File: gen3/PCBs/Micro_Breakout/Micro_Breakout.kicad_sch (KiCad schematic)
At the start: 50 parts, among them J1 BlueRobotics Depth Sensor, J10 Kill Switch, J11 StarOddi CTD Comms, J12 LED1, J13 LED2, J14 Leak Sensor, J15 Extra I2C #3, J16 Extra I2C #6, J17 Extra I2C #5, J18 Extra I2C #4, J19 GND Line, J2 Interconnect, J20 3.3V Line, J21 5V Line, J22 Extra SPI #1, J23 Extra SPI #2, J24 Extra SPI #3, J25 Secondary UART, J3 External Battery, J4 Conn_01x24, J5 External I2C, J6 Conn_01x24, J7 Extra I2C #1, J8 Extra I2C #2, J9 Lumen PWM, Q7 L78M05ABDT-TR, U15 AMS1117-3.3, U2 MCP9808_MSOP, U4 BME280, U6 Teensy4.1

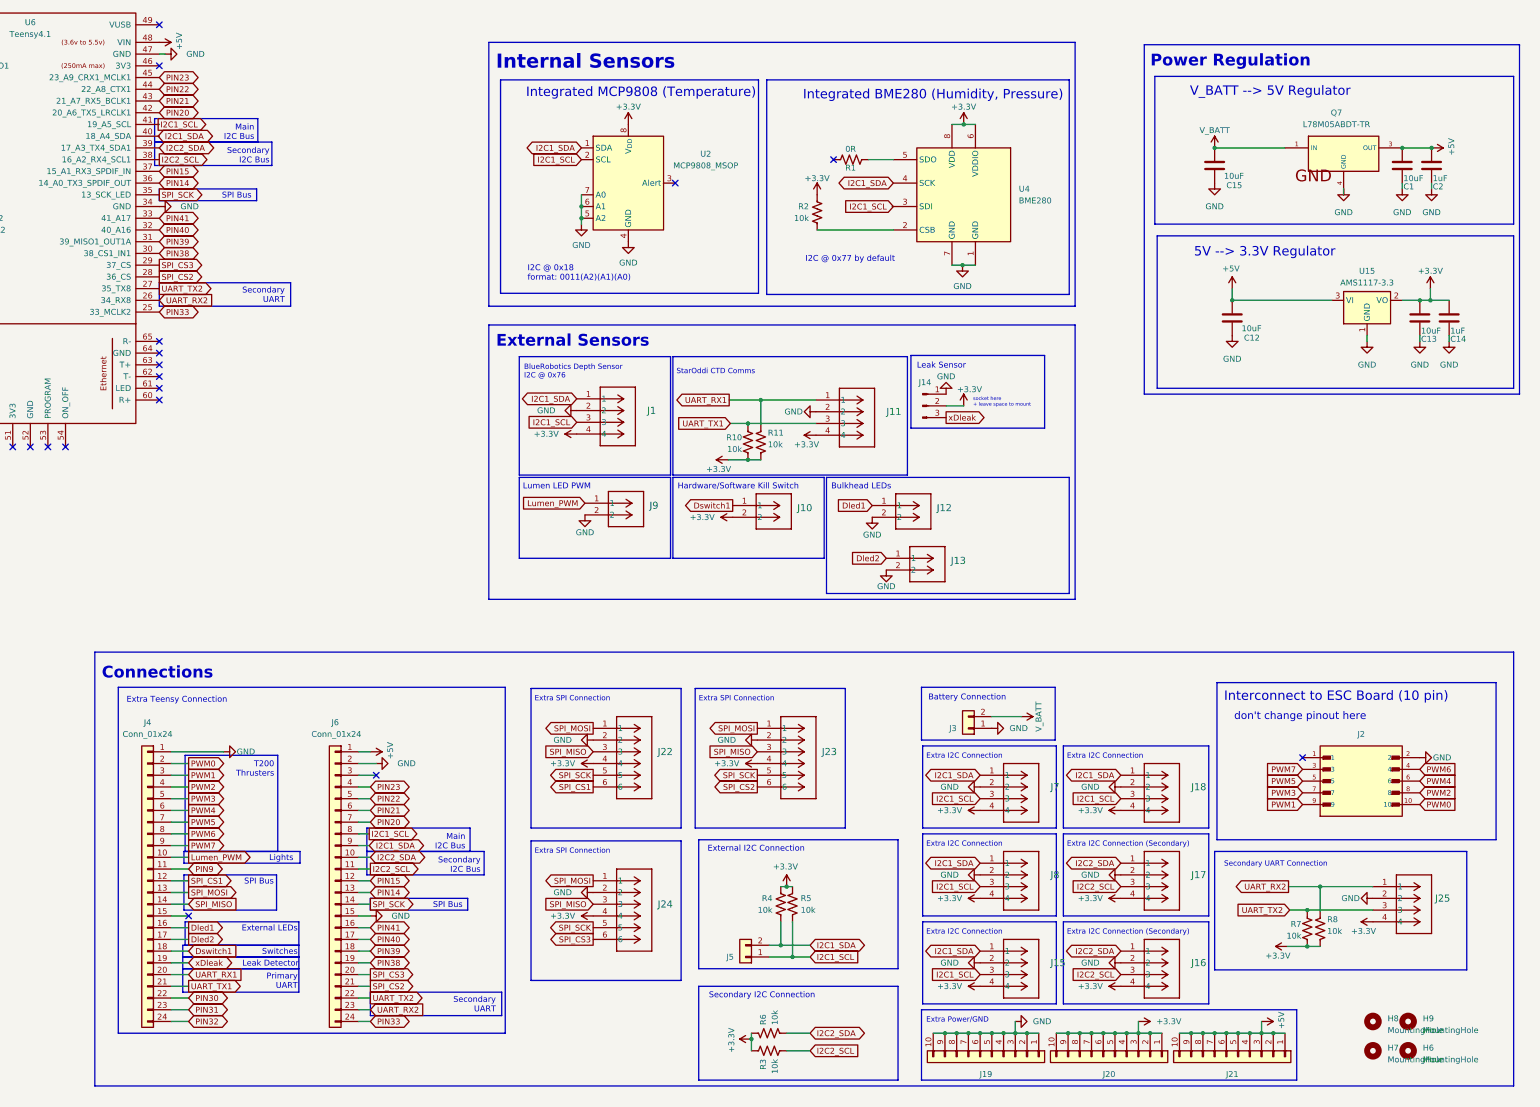
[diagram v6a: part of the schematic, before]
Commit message: added all custom in robosub_3d_models
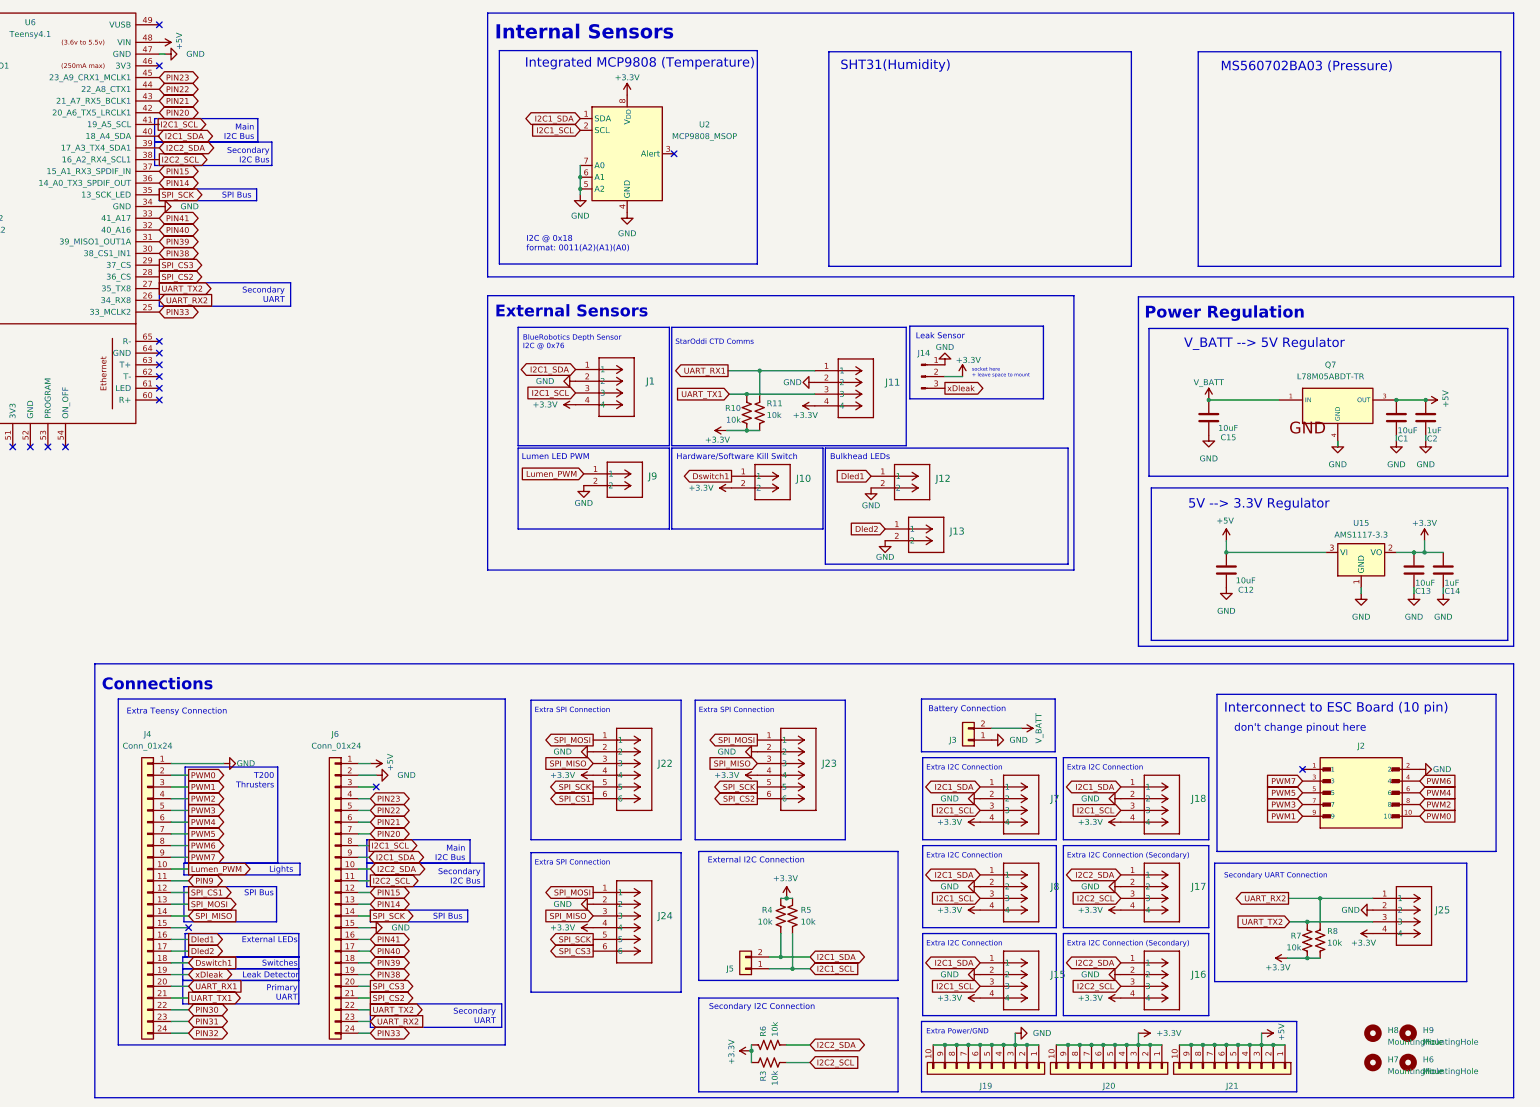
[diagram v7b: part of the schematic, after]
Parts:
- removed R1: 0R, Resistor_SMD:R_0805_2012Metric_Pad1.20x1.40mm_HandSolder, symbol Device:R_US
- removed R2: 10k, Resistor_SMD:R_0805_2012Metric_Pad1.20x1.40mm_HandSolder, symbol Device:R_US
- removed U4: BME280, Package_LGA:Bosch_LGA-8_2.5x2.5mm_P0.65mm_ClockwisePinNumbering, symbol Sensor:BME280
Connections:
- no-connect marks 26 -> 25
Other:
- note added: "MS560702BA03 (Pressure)"
- note added: "SHT31(Humidity)"
- note removed: "I2C @ 0x77 by default"
- note removed: "Integrated BME280 (Humidity, Pressure)"
- moved on the sheet: C1, C12, C13, C14, C15, C2, H6, H7, H8, H9, J1, J10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

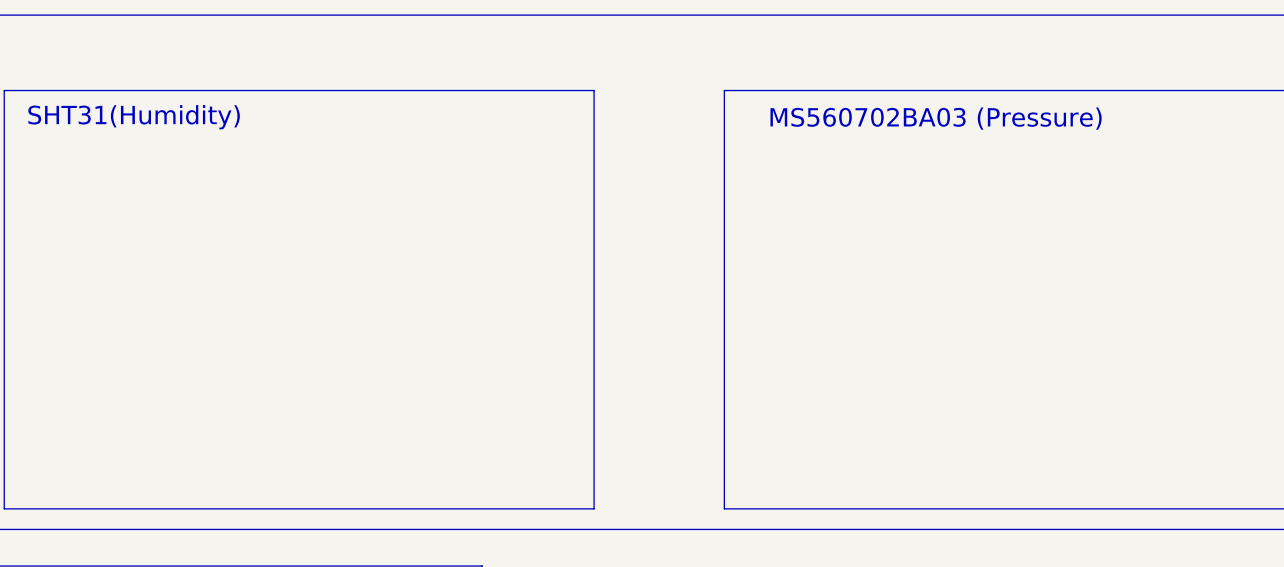
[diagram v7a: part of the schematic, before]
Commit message: no errors for updating symbol
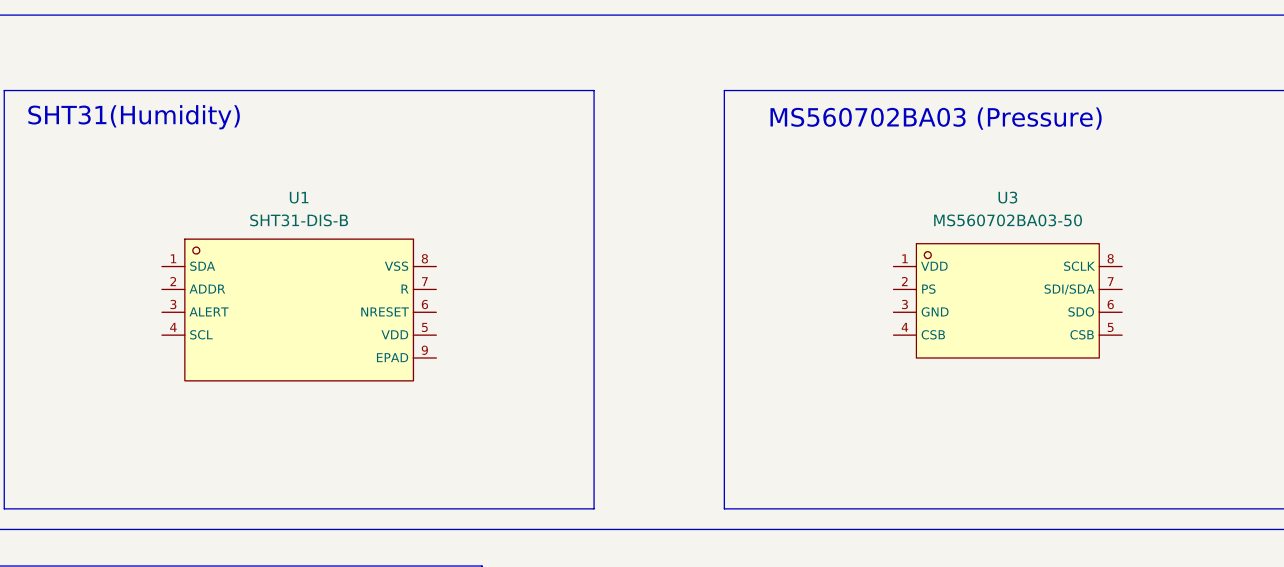
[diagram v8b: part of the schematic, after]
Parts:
- added U1: SHT31-DIS-B, robosub_footprints:DFN-8_L2.5-W2.5-P0.50-BL-EP, symbol robosub_symbols:SHT31-DIS-B
- added U3: MS560702BA03-50, robosub_footprints:SENSOR-SMD_MS560702BA03-50, symbol robosub_symbols:MS560702BA03-50
- J1, J11, J15, J16, J17, J18, J25, J7, J8: footprint Imported_Footprints:CONN_SD-43045-005_04_MOL -> robosub_footprints:CONN_SD-43045-008_04_MOL; symbol Imported:430450422 -> robosub_symbols:430450422
- J10, J12, J13, J9: footprint Imported_Footprints:CONN_SD-43045-005_02_MOL -> robosub_footprints:CONN_SD-43045-010_02_MOL; symbol Imported:430450228 -> robosub_symbols:430450228
- J2: footprint Imported_Footprints:SULLINS_SBH11-PBPC-D05-ST-BK -> robosub_footprints:SULLINS_SBH11-PBPC-D05-ST-BK; symbol Imported:SBH11-PBPC-D05-ST-BK -> robosub_symbols:SBH11-PBPC-D05-ST-BK
- J22, J23, J24: footprint Imported_Footprints:CONN_SD-43045-005_06_MOL -> robosub_footprints:CONN_SD-43045-005_06_MOL; symbol CONN_SD-43045-008_06_MOL:430450612 -> robosub_symbols:430450612
- Q7: symbol L78M05ABDT-TR:L78M05ABDT-TR -> robosub_symbols:L78M05ABDT-TR
- U6: symbol teensy:Teensy4.1 -> robosub_symbols:Teensy4.1
